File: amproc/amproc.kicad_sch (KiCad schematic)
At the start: 5 parts

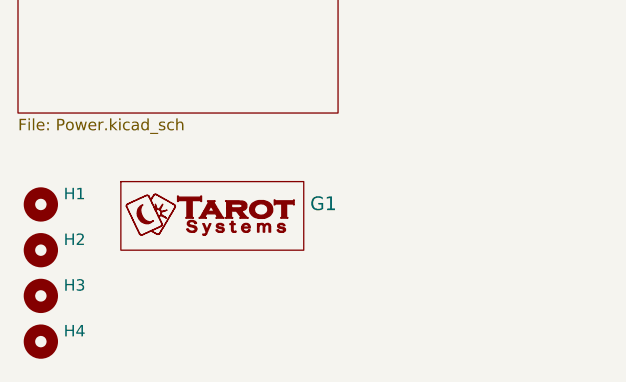
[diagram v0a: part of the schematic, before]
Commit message: Fix U8, U9 pinouts
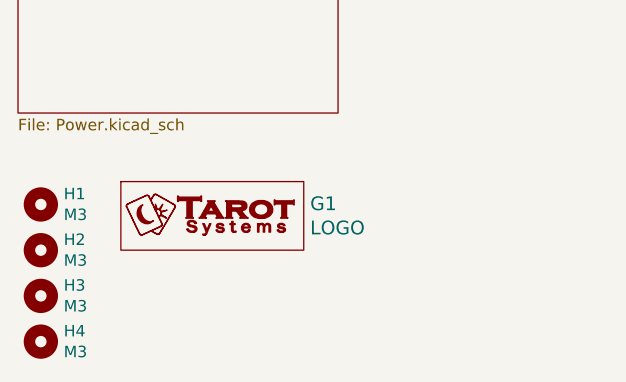
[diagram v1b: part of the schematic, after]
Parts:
- G1: value (none) -> LOGO; footprint (none) -> tarot:tarot_logo_fsilk_25mm
- H1, H2, H3, H4: value (none) -> M3; footprint (none) -> Mounting_Holes:MountingHole_3.2mm_M3
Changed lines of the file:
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@@
       (effects (font (size 1.524 1.524)) (justify left))
     )
-    (property "Value" "" (id 1) (at 64.2112 130.8862 0)
+    (property "Value" "LOGO" (id 1) (at 64.2112 130.8862 0)
       (effects (font (size 1.524 1.524)) (justify left))
     )
-    (property "Footprint" "" (id 2) (at 53.34 129.54 0)
+    (property "Footprint" "tarot:tarot_logo_fsilk_25mm" (id 2) (at 53.34 129.54 0)
       (effects (font (size 1.27 1.27)) hide)
     )
@@
       (effects (font (size 1.27 1.27)) (justify left))
     )
-    (property "Value" "" (id 1) (at 36.83 129.413 0)
-      (effects (font (size 1.27 1.27)) (justify left))
-    )
-    (property "Footprint" "" (id 2) (at 34.29 128.27 0)
+    (property "Value" "M3" (id 1) (at 36.83 129.413 0)
+      (effects (font (size 1.27 1.27)) (justify left))
+    )
+    (property "Footprint" "Mounting_Holes:MountingHole_3.2mm_M3" (id 2) (at 34.29 128.27 0)
       (effects (font (size 1.27 1.27)) hide)
     )
@@
       (effects (font (size 1.27 1.27)) (justify left))
     )
-    (property "Value" "" (id 1) (at 36.83 134.493 0)
-      (effects (font (size 1.27 1.27)) (justify left))
-    )
-    (property "Footprint" "" (id 2) (at 34.29 133.35 0)
+    (property "Value" "M3" (id 1) (at 36.83 134.493 0)
+      (effects (font (size 1.27 1.27)) (justify left))
+    )
+    (property "Footprint" "Mounting_Holes:MountingHole_3.2mm_M3" (id 2) (at 34.29 133.35 0)
       (effects (font (size 1.27 1.27)) hide)
     )
@@
       (effects (font (size 1.27 1.27)) (justify left))
     )
-    (property "Value" "" (id 1) (at 36.83 139.573 0)
-      (effects (font (size 1.27 1.27)) (justify left))
-    )
-    (property "Footprint" "" (id 2) (at 34.29 138.43 0)
+    (property "Value" "M3" (id 1) (at 36.83 139.573 0)
+      (effects (font (size 1.27 1.27)) (justify left))
+    )
+    (property "Footprint" "Mounting_Holes:MountingHole_3.2mm_M3" (id 2) (at 34.29 138.43 0)
       (effects (font (size 1.27 1.27)) hide)
     )
@@
       (effects (font (size 1.27 1.27)) (justify left))
     )
-    (property "Value" "" (id 1) (at 36.83 144.653 0)
-      (effects (font (size 1.27 1.27)) (justify left))
-    )
-    (property "Footprint" "" (id 2) (at 34.29 143.51 0)
+    (property "Value" "M3" (id 1) (at 36.83 144.653 0)
+      (effects (font (size 1.27 1.27)) (justify left))
+    )
+    (property "Footprint" "Mounting_Holes:MountingHole_3.2mm_M3" (id 2) (at 34.29 143.51 0)
       (effects (font (size 1.27 1.27)) hide)
     )
@@
     )
     (path "/00000000-0000-0000-0000-0000601b6abc/00000000-0000-0000-0000-0000601ba650"
-      (reference "U8") (unit 1) (value "L7815") (footprint "TO_SOT_Packages_THT:TO-220-3_Horizontal")
+      (reference "U8") (unit 1) (value "L7815") (footprint "Package_TO_SOT_THT:TO-220-3_Horizontal_TabUp")
     )
     (path "/00000000-0000-0000-0000-0000601b6abc/00000000-0000-0000-0000-0000601be9d6"
-      (reference "U9") (unit 1) (value "L7915") (footprint "TO_SOT_Packages_THT:TO-220-3_Horizontal")
-    )
-  )
+      (reference "U9") (unit 1) (value "L7915") (footprint "Package_TO_SOT_THT:TO-220-3_Horizontal_TabUp")
+    )
+  )
